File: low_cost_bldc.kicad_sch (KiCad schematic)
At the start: 14 parts, among them P1 USB_C_Plug_USB2.0

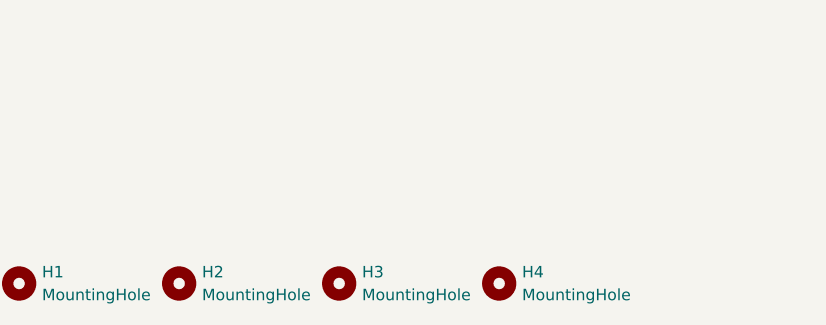
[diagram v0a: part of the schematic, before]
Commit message: Rough sketch-up of idea. Does introduce the problem of cooling the FETs now...
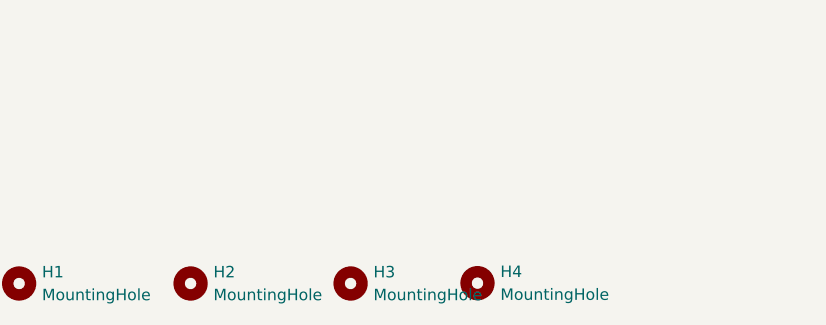
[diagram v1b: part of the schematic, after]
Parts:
- H1, H2, H3, H4: footprint MountingHole:MountingHole_3.2mm_M3 -> MountingHole:MountingHole_2.7mm_M2.5
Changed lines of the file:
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@@
-	)
-	(symbol
-		(lib_id "Mechanical:MountingHole")
-		(at 127 165.1 0)
-		(unit 1)
-		(exclude_from_sim yes)
-		(in_bom no)
-		(on_board yes)
-		(dnp no)
-		(fields_autoplaced yes)
-		(property "Reference" "H3"
-			(at 129.54 163.8299 0)
-			(effects
-				(font
-					(size 1.27 1.27)
-				)
-				(justify left)
-			)
-		)
-		(property "Value" "MountingHole"
-			(at 129.54 166.3699 0)
-			(effects
-				(font
-					(size 1.27 1.27)
-				)
-				(justify left)
-			)
-		)
-		(property "Footprint" "MountingHole:MountingHole_3.2mm_M3"
-			(at 127 165.1 0)
-			(effects
-				(font
-					(size 1.27 1.27)
-				)
-				(hide yes)
-			)
-		)
-		(property "Datasheet" "~"
-			(at 127 165.1 0)
-			(effects
-				(font
-					(size 1.27 1.27)
-				)
-				(hide yes)
-			)
-		)
-		(property "Description" "Mounting Hole without connection"
-			(at 127 165.1 0)
-			(effects
-				(font
-					(size 1.27 1.27)
-				)
-				(hide yes)
-			)
-		)
-		(instances
-			(project "low_cost_bldc"
-				(path "/e565d448-f724-46fc-88a0-0a0a0cb7460c"
-					(reference "H3")
-					(unit 1)
-				)
-			)
-		)
 	)
 	(symbol
@@
 			)
 		)
-		(property "Footprint" "MountingHole:MountingHole_3.2mm_M3"
+		(property "Footprint" "MountingHole:MountingHole_2.7mm_M2.5"
 			(at 91.44 165.1 0)
 			(effects
@@
 	(symbol
 		(lib_id "Mechanical:MountingHole")
-		(at 109.22 165.1 0)
+		(at 110.49 165.1 0)
 		(unit 1)
 		(exclude_from_sim yes)
@@
 		(fields_autoplaced yes)
 		(property "Reference" "H2"
-			(at 111.76 163.8299 0)
+			(at 113.03 163.8299 0)
 			(effects
 				(font
@@
 		)
 		(property "Value" "MountingHole"
-			(at 111.76 166.3699 0)
-			(effects
-				(font
-					(size 1.27 1.27)
-				)
-				(justify left)
-			)
-		)
-		(property "Footprint" "MountingHole:MountingHole_3.2mm_M3"
-			(at 109.22 165.1 0)
-			(effects
-				(font
-					(size 1.27 1.27)
-				)
-				(hide yes)
-			)
-		)
-		(property "Datasheet" "~"
-			(at 109.22 165.1 0)
+			(at 113.03 166.3699 0)
+			(effects
+				(font
+					(size 1.27 1.27)
+				)
+				(justify left)
+			)
+		)
+		(property "Footprint" "MountingHole:MountingHole_2.7mm_M2.5"
+			(at 110.49 165.1 0)
+			(effects
+				(font
+					(size 1.27 1.27)
+				)
+				(hide yes)
+			)
+		)
+		(property "Datasheet" "~"
+			(at 110.49 165.1 0)
 			(effects
 				(font
@@
 		)
 		(property "Description" "Mounting Hole without connection"
-			(at 109.22 165.1 0)
+			(at 110.49 165.1 0)
 			(effects
 				(font
@@
 				(path "/e565d448-f724-46fc-88a0-0a0a0cb7460c"
 					(reference "C4")
+					(unit 1)
+				)
+			)
+		)
+	)
+	(symbol
+		(lib_id "Mechanical:MountingHole")
+		(at 142.3711 165.0614 0)
+		(unit 1)
+		(exclude_from_sim yes)
+		(in_bom no)
+		(on_board yes)
+		(dnp no)
+		(fields_autoplaced yes)
+		(property "Reference" "H4"
+			(at 144.9111 163.7913 0)
+			(effects
+				(font
+					(size 1.27 1.27)
+				)
+				(justify left)
+			)
+		)
+		(property "Value" "MountingHole"
+			(at 144.9111 166.3313 0)
+			(effects
+				(font
+					(size 1.27 1.27)
+				)
+				(justify left)
+			)
+		)
+		(property "Footprint" "MountingHole:MountingHole_2.7mm_M2.5"
+			(at 142.3711 165.0614 0)
+			(effects
+				(font
+					(size 1.27 1.27)
+				)
+				(hide yes)
+			)
+		)
+		(property "Datasheet" "~"
+			(at 142.3711 165.0614 0)
+			(effects
+				(font
+					(size 1.27 1.27)
+				)
+				(hide yes)
+			)
+		)
+		(property "Description" "Mounting Hole without connection"
+			(at 142.3711 165.0614 0)
+			(effects
+				(font
+					(size 1.27 1.27)
+				)
+				(hide yes)
+			)
+		)
+		(instances
+			(project "low_cost_bldc"
+				(path "/e565d448-f724-46fc-88a0-0a0a0cb7460c"
+					(reference "H4")
 					(unit 1)
 				)
@@
 	)
 	(symbol
+		(lib_id "Device:C")
+		(at 135.89 39.37 0)
+		(unit 1)
+		(exclude_from_sim no)
+		(in_bom yes)
+		(on_board yes)
+		(dnp no)
+		(property "Reference" "C1"
+			(at 137.16 36.576 0)
+			(effects
+				(font
+					(size 1.27 1.27)
+				)
+				(justify left)
+			)
+		)
+		(property "Value" "10uF"
+			(at 137.16 41.91 0)
+			(effects
+				(font
+					(size 1.27 1.27)
+				)
+				(justify left)
+			)
+		)
+		(property "Footprint" "Capacitor_SMD:C_1206_3216Metric"
+			(at 136.8552 43.18 0)
+			(effects
+				(font
+					(size 1.27 1.27)
+				)
+				(hide yes)
+			)
+		)
+		(property "Datasheet" "~"
+			(at 135.89 39.37 0)
+			(effects
+				(font
+					(size 1.27 1.27)
+				)
+				(hide yes)
+			)
+		)
+		(property "Description" "Unpolarized capacitor"
+			(at 143.764 42.926 0)
+			(effects
+				(font
+					(size 1.27 1.27)
+					(color 0 132 132 1)
+				)
+				(hide yes)
+			)
+		)
+		(pin "1"
+		)
+		(pin "2"
+		)
+		(instances
+			(project "low_cost_bldc"
+				(path "/e565d448-f724-46fc-88a0-0a0a0cb7460c"
+					(reference "C1")
+					(unit 1)
+				)
+			)
+		)
+	)
+	(symbol
 		(lib_id "Mechanical:MountingHole")
-		(at 144.78 165.1 0)
+		(at 128.27 165.1 0)
 		(unit 1)
 		(exclude_from_sim yes)
@@
 		(dnp no)
 		(fields_autoplaced yes)
-		(property "Reference" "H4"
-			(at 147.32 163.8299 0)
+		(property "Reference" "H3"
+			(at 130.81 163.8299 0)
 			(effects
 				(font
@@
 		)
 		(property "Value" "MountingHole"
-			(at 147.32 166.3699 0)
-			(effects
-				(font
-					(size 1.27 1.27)
-				)
-				(justify left)
-			)
-		)
-		(property "Footprint" "MountingHole:MountingHole_3.2mm_M3"
-			(at 144.78 165.1 0)
-			(effects
-				(font
-					(size 1.27 1.27)
-				)
-				(hide yes)
-			)
-		)
-		(property "Datasheet" "~"
-			(at 144.78 165.1 0)
+			(at 130.81 166.3699 0)
+			(effects
+				(font
+					(size 1.27 1.27)
+				)
+				(justify left)
+			)
+		)
+		(property "Footprint" "MountingHole:MountingHole_2.7mm_M2.5"
+			(at 128.27 165.1 0)
+			(effects
+				(font
+					(size 1.27 1.27)
+				)
+				(hide yes)
+			)
+		)
+		(property "Datasheet" "~"
+			(at 128.27 165.1 0)
 			(effects
 				(font
@@
 		)
 		(property "Description" "Mounting Hole without connection"
-			(at 144.78 165.1 0)
-			(effects
-				(font
-					(size 1.27 1.27)
-				)
-				(hide yes)
-			)
-		)
-		(instances
-			(project "low_cost_bldc"
-				(path "/e565d448-f724-46fc-88a0-0a0a0cb7460c"
-					(reference "H4")
-					(unit 1)
-				)
-			)
-		)
-	)
-	(symbol
-		(lib_id "Device:C")
-		(at 135.89 39.37 0)
-		(unit 1)
-		(exclude_from_sim no)
-		(in_bom yes)
-		(on_board yes)
-		(dnp no)
-		(property "Reference" "C1"
-			(at 137.16 36.576 0)
-			(effects
-				(font
-					(size 1.27 1.27)
-				)
-				(justify left)
-			)
-		)
-		(property "Value" "10uF"
-			(at 137.16 41.91 0)
-			(effects
-				(font
-					(size 1.27 1.27)
-				)
-				(justify left)
-			)
-		)
-		(property "Footprint" "Capacitor_SMD:C_1206_3216Metric"
-			(at 136.8552 43.18 0)
-			(effects
-				(font
-					(size 1.27 1.27)
-				)
-				(hide yes)
-			)
-		)
-		(property "Datasheet" "~"
-			(at 135.89 39.37 0)
-			(effects
-				(font
-					(size 1.27 1.27)
-				)
-				(hide yes)
-			)
-		)
-		(property "Description" "Unpolarized capacitor"
-			(at 143.764 42.926 0)
-			(effects
-				(font
-					(size 1.27 1.27)
-					(color 0 132 132 1)
-				)
-				(hide yes)
-			)
-		)
-		(pin "1"
-		)
-		(pin "2"
-		)
-		(instances
-			(project "low_cost_bldc"
-				(path "/e565d448-f724-46fc-88a0-0a0a0cb7460c"
-					(reference "C1")
-					(unit 1)
-				)
+			(at 128.27 165.1 0)
+			(effects
+				(font
+					(size 1.27 1.27)
+				)
+				(hide yes)
+			)
+		)
+		(instances
+			(project "low_cost_bldc"
+				(path "/e565d448-f724-46fc-88a0-0a0a0cb7460c"
+					(reference "H3")
+					(unit 1)
+				)
